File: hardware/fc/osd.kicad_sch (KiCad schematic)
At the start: 17 parts, among them U11 OPA354AIDBVR, U8 TS5A3159ADCK, U9 TLV7031DCKR

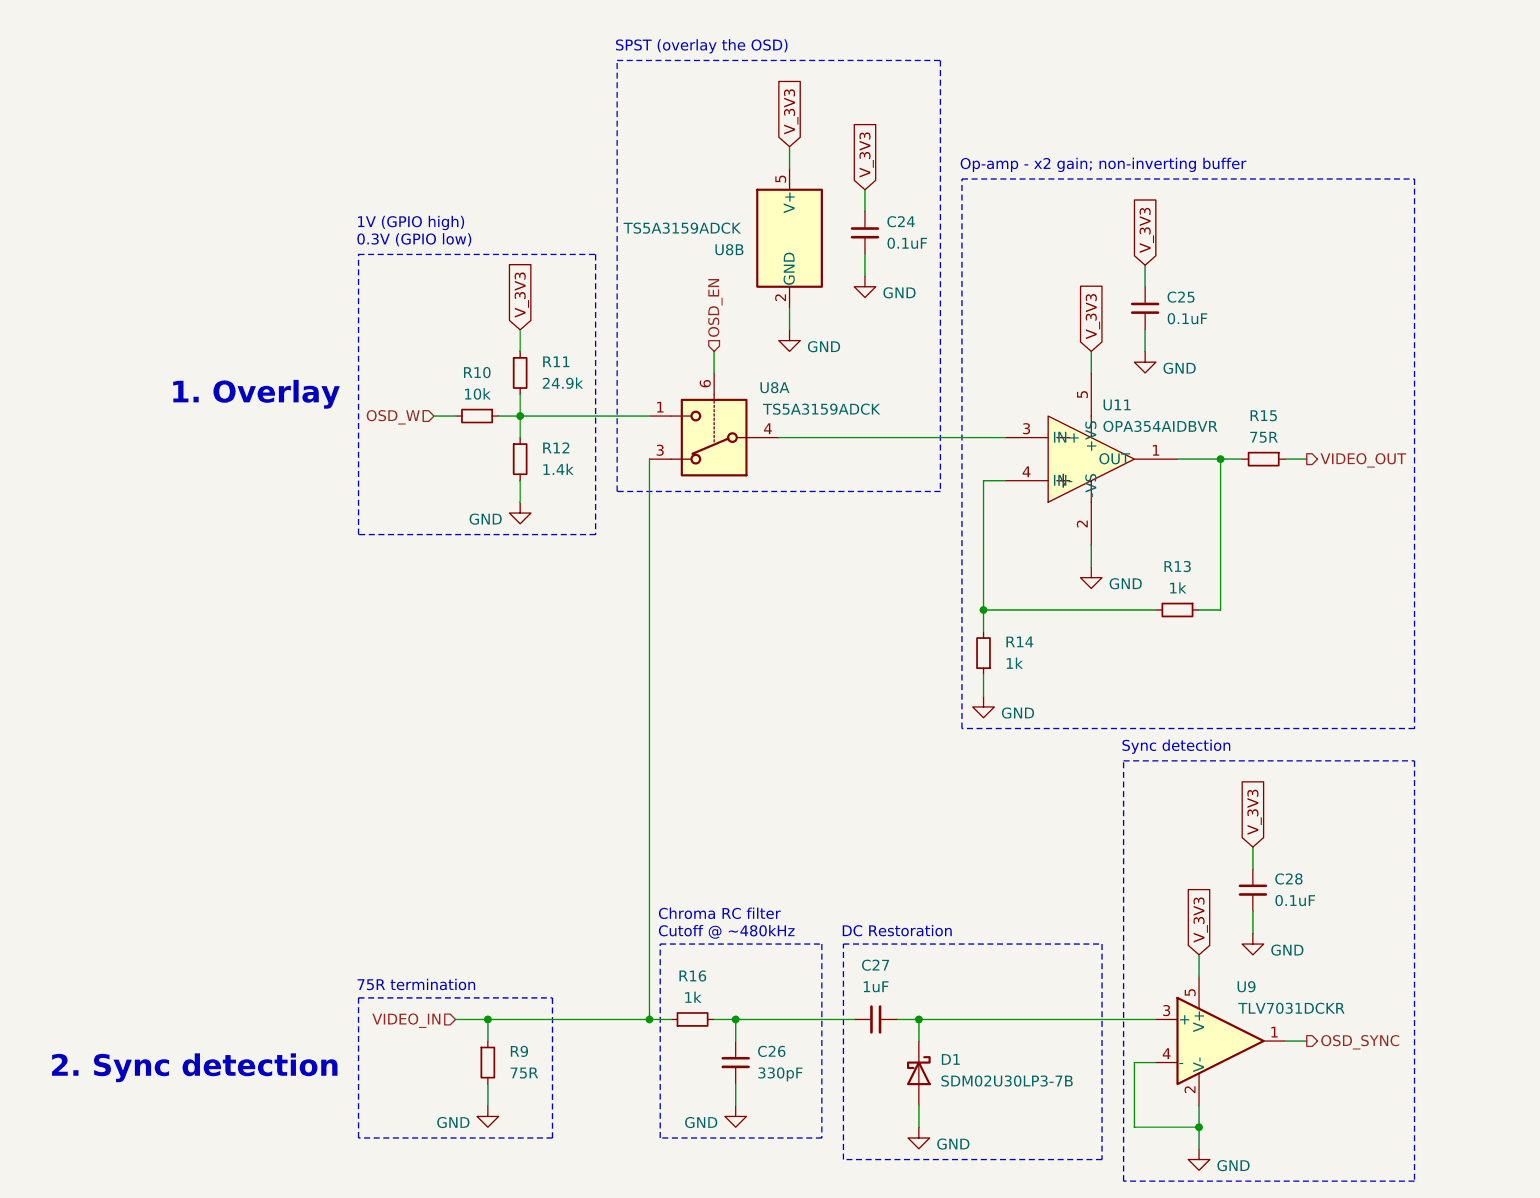
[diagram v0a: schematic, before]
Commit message: fc: update formatting; route RP2354 passives
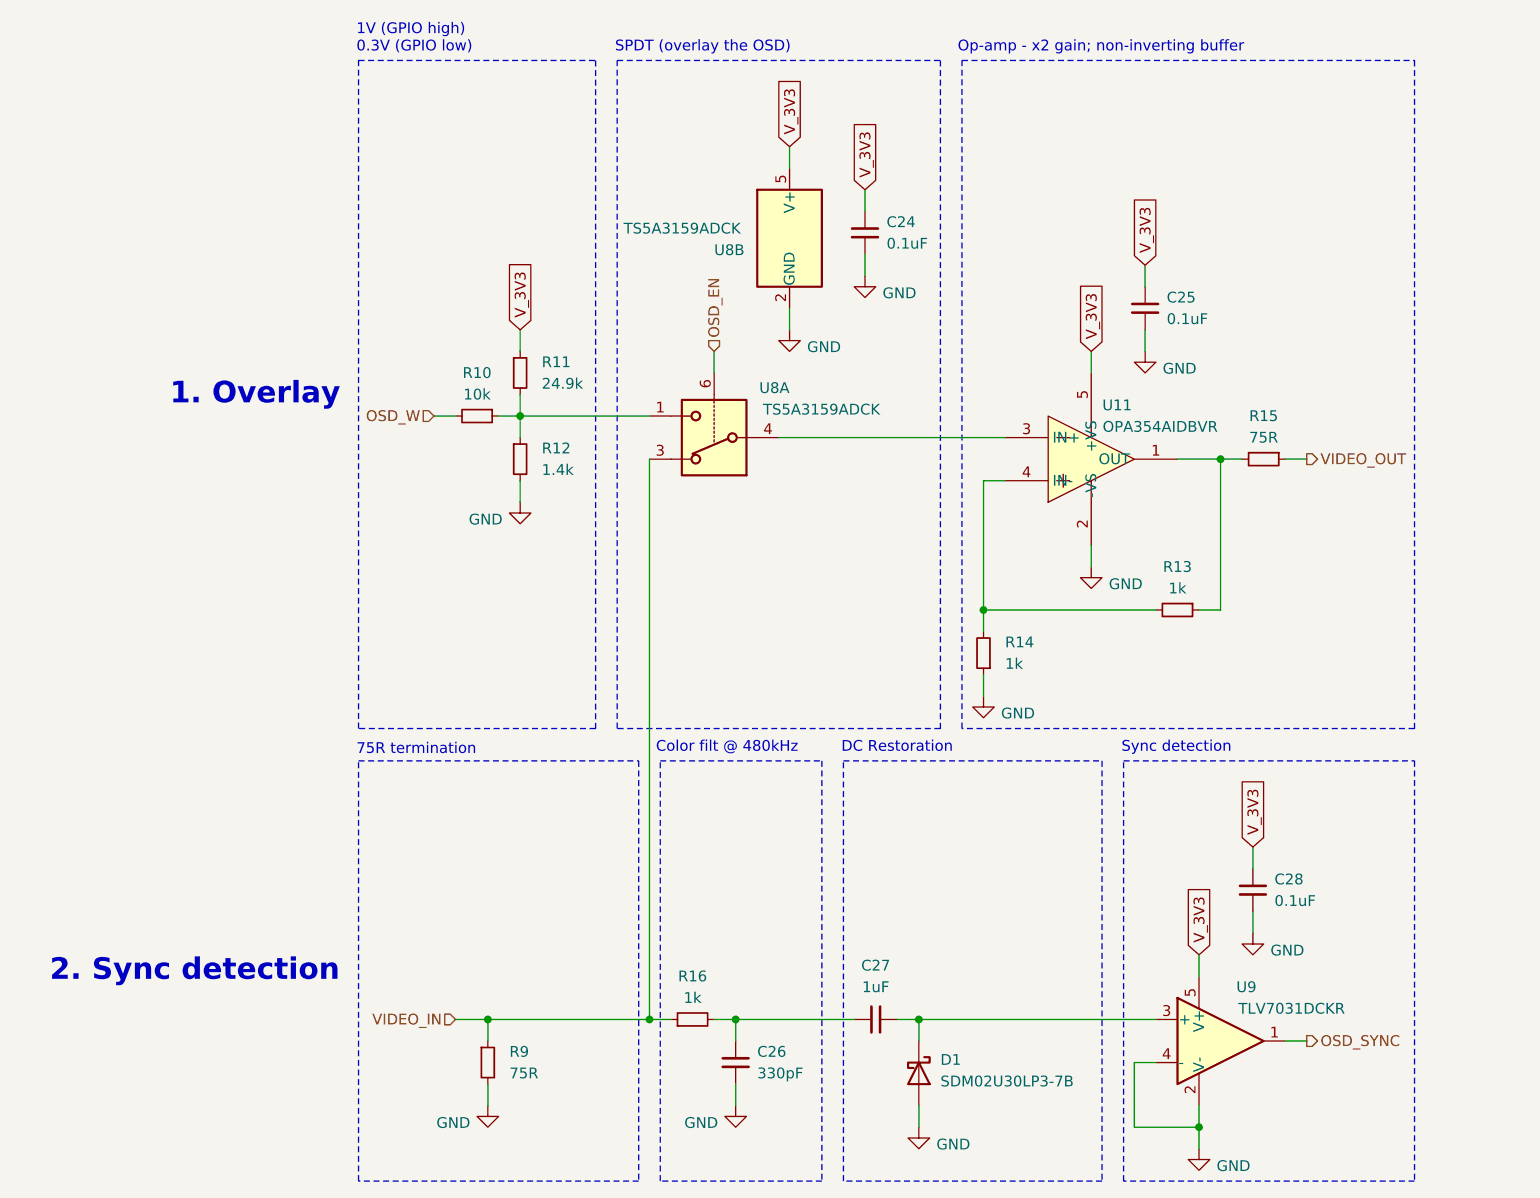
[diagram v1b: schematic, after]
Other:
- note added: "Color filt @ 480kHz"
- note added: "SPDT (overlay the OSD)"
- note removed: "Chroma RC filter Cutoff @ ~480kHz"
- note removed: "SPST (overlay the OSD)"
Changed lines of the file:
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@@
 	)
 	(rectangle
-		(start 162.56 38.1)
+		(start 162.56 24.13)
 		(end 215.9 102.87)
 		(stroke
@@
 	)
 	(rectangle
-		(start 127 128.27)
-		(end 146.05 151.13)
+		(start 127 106.68)
+		(end 146.05 156.21)
 		(stroke
 			(width 0)
@@
 	)
 	(rectangle
-		(start 91.44 46.99)
-		(end 119.38 80.01)
+		(start 91.44 24.13)
+		(end 119.38 102.87)
 		(stroke
 			(width 0)
@@
 	)
 	(rectangle
-		(start 148.59 128.27)
-		(end 179.07 153.67)
+		(start 148.59 106.68)
+		(end 179.07 156.21)
 		(stroke
 			(width 0)
@@
 	(rectangle
 		(start 121.92 24.13)
-		(end 160.02 74.93)
+		(end 160.02 102.87)
 		(stroke
 			(width 0)
@@
 	)
 	(rectangle
-		(start 91.44 134.62)
-		(end 114.3 151.13)
+		(start 91.44 106.68)
+		(end 124.46 156.21)
 		(stroke
 			(width 0)
@@
 	(text "75R termination"
 		(exclude_from_sim no)
-		(at 91.186 133.35 0)
+		(at 91.186 105.41 0)
 		(effects
 			(font
@@
 	(text "Op-amp - x2 gain; non-inverting buffer"
 		(exclude_from_sim no)
-		(at 162.306 36.576 0)
+		(at 162.052 22.606 0)
 		(effects
 			(font
@@
 	(text "2. Sync detection"
 		(exclude_from_sim no)
-		(at 72.136 142.875 0)
+		(at 72.136 131.445 0)
 		(effects
 			(font
@@
 	(text "1V (GPIO high)\n0.3V (GPIO low)"
 		(exclude_from_sim no)
-		(at 91.186 44.45 0)
+		(at 91.186 21.59 0)
 		(effects
 			(font
@@
 		)
 	)
-	(text "Chroma RC filter\nCutoff @ ~480kHz\n"
+	(text "Color filt @ 480kHz\n"
 		(exclude_from_sim no)
-		(at 126.746 125.984 0)
+		(at 126.492 105.156 0)
 		(effects
 			(font
@@
 	(text "DC Restoration"
 		(exclude_from_sim no)
-		(at 148.336 127 0)
+		(at 148.336 105.156 0)
 		(effects
 			(font
@@
 		)
 	)
-	(text "SPST (overlay the OSD)"
+	(text "SPDT (overlay the OSD)"
 		(exclude_from_sim no)
 		(at 121.666 22.606 0)

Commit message: fc: add footprints
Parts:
- C24, C25, C26, C28: footprint Package_TO_SOT_SMD:SOT-363_SC-70-6 -> Stratus:C_0402
- C27: footprint (none) -> Stratus:C_0402
- D1: value SDM02U30LP3-7B -> SDM10U45LP-7; footprint Package_TO_SOT_SMD:SOT-363_SC-70-6 -> Diode_SMD:D_SOD-882
- R10, R11, R12, R13, R14, R15, R16, R9: footprint (none) -> Stratus:R_0402
- U11: footprint lib:SOT-23-5_L3.0-W1.7-P0.95-LS2.8-BR -> Package_TO_SOT_SMD:SOT-23-5
- U9: footprint Package_TO_SOT_SMD:SOT-23-5 -> Package_TO_SOT_SMD:SOT-363_SC-70-6
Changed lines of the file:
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@@
 			)
 		)
-		(property "Footprint" ""
+		(property "Footprint" "Stratus:R_0402"
 			(at 165.1 93.98 0)
 			(hide yes)
@@
 			)
 		)
-		(property "Footprint" "Package_TO_SOT_SMD:SOT-363_SC-70-6"
+		(property "Footprint" "Stratus:C_0402"
 			(at 151.13 44.45 0)
 			(hide yes)
@@
 			)
 		)
-		(property "Footprint" "Package_TO_SOT_SMD:SOT-363_SC-70-6"
+		(property "Footprint" "Stratus:C_0402"
 			(at 135.89 142.24 0)
 			(hide yes)
@@
 			)
 		)
-		(property "Footprint" ""
+		(property "Footprint" "Stratus:R_0402"
 			(at 105.41 66.04 0)
 			(hide yes)
@@
 			)
 		)
-		(property "Footprint" ""
+		(property "Footprint" "Stratus:R_0402"
 			(at 187.96 88.9 0)
 			(hide yes)
@@
 			)
 		)
-		(property "Footprint" "Package_TO_SOT_SMD:SOT-23-5"
+		(property "Footprint" "Package_TO_SOT_SMD:SOT-363_SC-70-6"
 			(at 190.5 144.78 0)
 			(hide yes)
@@
 			)
 		)
-		(property "Footprint" "Package_TO_SOT_SMD:SOT-363_SC-70-6"
+		(property "Footprint" "Stratus:C_0402"
 			(at 196.85 121.92 0)
 			(hide yes)
@@
 			)
 		)
-		(property "Footprint" ""
+		(property "Footprint" "Stratus:C_0402"
 			(at 152.4 137.16 0)
 			(hide yes)
@@
 			)
 		)
-		(property "Footprint" "Package_TO_SOT_SMD:SOT-363_SC-70-6"
+		(property "Footprint" "Stratus:C_0402"
 			(at 184.15 53.34 0)
 			(hide yes)
@@
 			)
 		)
-		(property "Value" "SDM02U30LP3-7B"
+		(property "Value" "SDM10U45LP-7"
 			(at 160.02 144.4624 90)
 			(show_name no)
@@
 			)
 		)
-		(property "Footprint" "Package_TO_SOT_SMD:SOT-363_SC-70-6"
+		(property "Footprint" "Diode_SMD:D_SOD-882"
 			(at 157.48 143.51 0)
 			(hide yes)
@@
 			)
 		)
-		(property "Footprint" ""
+		(property "Footprint" "Stratus:R_0402"
 			(at 106.68 142.24 0)
 			(hide yes)
@@
 			)
 		)
-		(property "Footprint" ""
+		(property "Footprint" "Stratus:R_0402"
 			(at 110.49 71.12 0)
 			(hide yes)
@@
 			)
 		)
-		(property "Footprint" ""
+		(property "Footprint" "Stratus:R_0402"
 			(at 110.49 60.96 0)
 			(hide yes)
@@
 			)
 		)
-		(property "Footprint" ""
+		(property "Footprint" "Stratus:R_0402"
 			(at 130.81 137.16 0)
 			(hide yes)
@@
 			)
 		)
-		(property "Footprint" "lib:SOT-23-5_L3.0-W1.7-P0.95-LS2.8-BR"
+		(property "Footprint" "Package_TO_SOT_SMD:SOT-23-5"
 			(at 177.8 88.9 0)
 			(hide yes)
@@
 			)
 		)
-		(property "Footprint" ""
+		(property "Footprint" "Stratus:R_0402"
 			(at 198.12 71.12 0)
 			(hide yes)

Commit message: fc: schematic tweaks; prelim power stage + connector layout
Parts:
- U9: footprint Package_TO_SOT_SMD:SOT-363_SC-70-6 -> Package_TO_SOT_SMD:SOT-353_SC-70-5
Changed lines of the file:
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@@
 			)
 		)
-		(property "Footprint" "Package_TO_SOT_SMD:SOT-363_SC-70-6"
+		(property "Footprint" "Package_TO_SOT_SMD:SOT-353_SC-70-5"
 			(at 190.5 144.78 0)
 			(hide yes)

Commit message: fc: footprints
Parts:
- D1: footprint Diode_SMD:D_SOD-882 -> Stratus:D_0402
- U11: footprint Package_TO_SOT_SMD:SOT-23-5 -> Stratus:OPA354AIDBVR
- U8: footprint Package_TO_SOT_SMD:SOT-363_SC-70-6 -> Stratus:TS5A3159ADCK
- U9: footprint Package_TO_SOT_SMD:SOT-353_SC-70-5 -> Stratus:TLV7031DCKR
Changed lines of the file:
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@@
 			)
 		)
-		(property "Footprint" "Package_TO_SOT_SMD:SOT-363_SC-70-6"
+		(property "Footprint" "Stratus:TS5A3159ADCK"
 			(at 142.875 54.61 0)
 			(hide yes)
@@
 			)
 		)
-		(property "Footprint" "Package_TO_SOT_SMD:SOT-353_SC-70-5"
+		(property "Footprint" "Stratus:TLV7031DCKR"
 			(at 190.5 144.78 0)
 			(hide yes)
@@
 			)
 		)
-		(property "Footprint" "Package_TO_SOT_SMD:SOT-363_SC-70-6"
+		(property "Footprint" "Stratus:TS5A3159ADCK"
 			(at 132.715 54.61 0)
 			(hide yes)
@@
 			)
 		)
-		(property "Footprint" "Diode_SMD:D_SOD-882"
+		(property "Footprint" "Stratus:D_0402"
 			(at 157.48 143.51 0)
 			(hide yes)
@@
 			)
 		)
-		(property "Footprint" "Package_TO_SOT_SMD:SOT-23-5"
+		(property "Footprint" "Stratus:OPA354AIDBVR"
 			(at 177.8 88.9 0)
 			(hide yes)

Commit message: fc: add rbleed, swap comparator, clamp video to vref
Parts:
- added C48: 0.1uF, Stratus:C_0402, symbol Device:C_Small
- added R28: 100k, Stratus:R_0402, symbol Device:R_Small
- added R29: 10k, Stratus:R_0402, symbol Device:R_Small
- added R30: 1.5k, Stratus:R_0402, symbol Device:R_Small
- R12: value 1.4k -> 3.24k
- U9: value TLV7031DCKR -> LMV7219M7X; footprint Stratus:TLV7031DCKR -> Stratus:LMV7219M7X_NOPB
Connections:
- net GND: now also C48.1, R28.2, R30.2; no longer D1.2 (A), U9.4 (-)
- net V_3V3: now also R29.1
- net at C27.1, D1.1 (K), U9.3 (+): now also R28.1
- new net V_REF: C48.2, D1.2 (A), R29.2, R30.1, U9.4 (-)
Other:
- moved on the sheet: C28, D1, U9

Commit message: fc: move DC restoration/clamp to shared path
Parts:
- R10: value 10k -> 2k
- R11: value 24.9k -> 3.09k
- R12: value 3.24k -> 649R
- R30: value 1.5k -> 1.2k
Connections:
- net VIDEO_IN: now also C27.2; no longer R16.1, U8.3
- net at C26.1, R16.2: now also U9.3 (+); no longer C27.2
- net at C27.1, D1.1 (K), R28.1: now also R16.1, U8.3; no longer U9.3 (+)
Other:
- note added: "1.15V (GPIO high) 0.45V (GPIO low)"
- note removed: "1V (GPIO high) 0.3V (GPIO low)"
- moved on the sheet: C27, C48, D1, R28, R29, R30

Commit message: fc: edit values to add temperature drift robustness to OSD
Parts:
- C27: value 1uF -> 0.1uF
- R28: value 100k -> 1M
- R30: value 1.2k -> 1k
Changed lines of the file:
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@@
 			)
 		)
-		(property "Value" "1.2k"
+		(property "Value" "1k"
 			(at 161.29 126.9999 0)
 			(show_name no)
@@
 			)
 		)
-		(property "Value" "100k"
+		(property "Value" "1M"
 			(at 138.43 143.5099 0)
 			(show_name no)
@@
 			)
 		)
-		(property "Value" "1uF"
+		(property "Value" "0.1uF"
 			(at 130.81 133.35 90)
 			(show_name no)

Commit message: fc: final resistor edit
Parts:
- R28: value 1M -> 220k
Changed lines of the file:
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@@
 			)
 		)
-		(property "Value" "1M"
+		(property "Value" "220k"
 			(at 138.43 143.5099 0)
 			(show_name no)
